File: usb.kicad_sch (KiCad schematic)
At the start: 7 parts, among them J3 USB_C_Plug, U2 STUSB03EQR

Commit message: *.kicad_sch: add CHIPSAlliance_ prefix for footprint
Signed-off-by: Huang Rui <vowstar@gmail.com>
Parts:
- U2: footprint Interface:QFN_B03EQR_STM -> CHIPSAlliance_Interface:QFN_B03EQR_STM
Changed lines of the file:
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@@
       (effects (font (size 1.524 1.524)))
     )
-    (property "Footprint" "Interface:QFN_B03EQR_STM" (at 76.2 100.33 0)
+    (property "Footprint" "CHIPSAlliance_Interface:QFN_B03EQR_STM" (at 76.2 100.33 0)
       (effects (font (size 1.524 1.524)) (justify left) hide)
     )

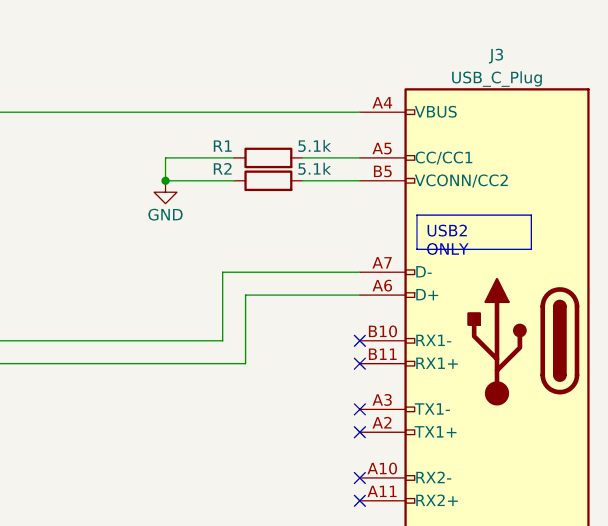
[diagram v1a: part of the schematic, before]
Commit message: library,uart*,usb*: fix usb connectors
Signed-off-by: Huang Rui <vowstar@gmail.com>
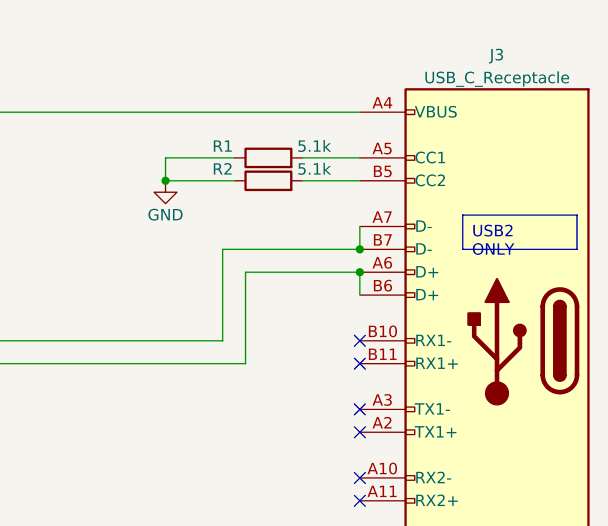
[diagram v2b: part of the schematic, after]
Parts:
- removed J3: USB_C_Plug, Connector_USB:USB_C_Receptacle_Molex_105450-0101, symbol CHIPSAlliance_Connector:USB_C_Plug
- added J3: USB_C_Receptacle, Connector_USB:USB_C_Receptacle_Molex_105450-0101, symbol CHIPSAlliance_Connector:USB_C_Receptacle
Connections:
- net D+: now also J3.A6 (D+), J3.B6 (D+)
- net D-: now also J3.A7 (D-), J3.B7 (D-)
- net GND: now also J3.A1 (GND), J3.A12 (GND), J3.B1 (GND), J3.B12 (GND), J3.S1 (SHIELD)
- net at R1.2: now also J3.A5 (CC1)
- net at C1.1, U2.14 (VBUS): now also J3.A4 (VBUS), J3.A9 (VBUS), J3.B4 (VBUS), J3.B9 (VBUS)
- net at R2.2: now also J3.B5 (CC2)

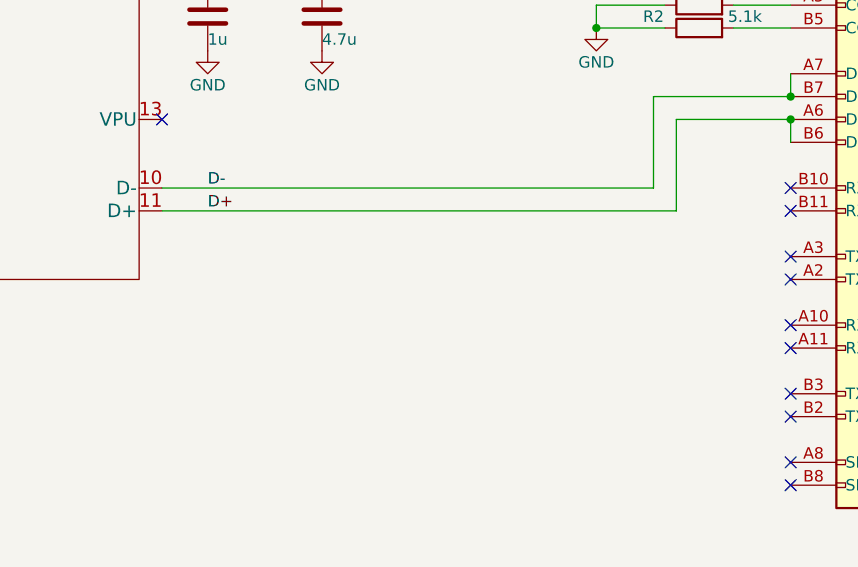
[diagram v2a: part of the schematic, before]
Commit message: {spi,uart,usb}.kicad_sch: add TPD4E02B04DQA as ESD protect
Signed-off-by: Huang Rui <vowstar@gmail.com>
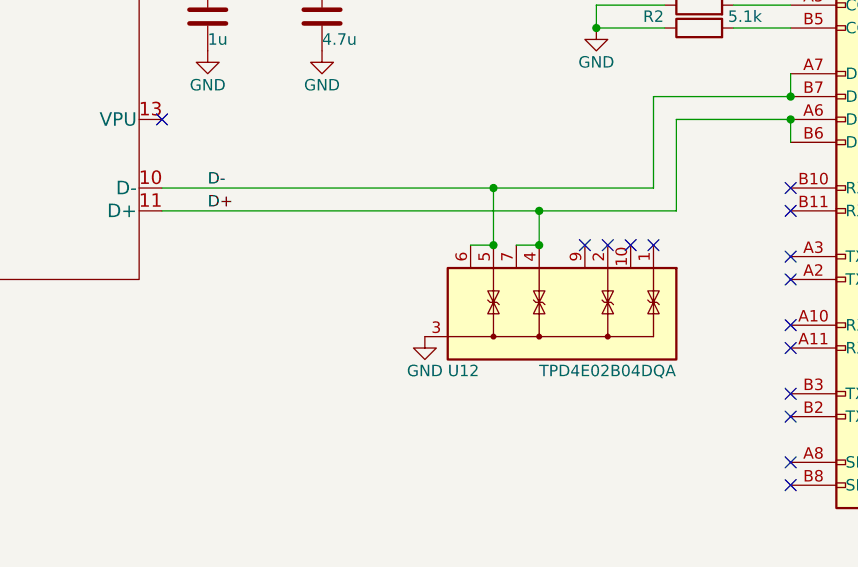
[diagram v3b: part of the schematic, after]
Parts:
- added U12: TPD4E02B04DQA, Package_SON:USON-10_2.5x1.0mm_P0.5mm, symbol Power_Protection:TPD4E02B04DQA
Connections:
- net D+: now also U12.4 (IO3), U12.7 (NC)
- net D-: now also U12.5 (IO4), U12.6 (NC)
- net GND: now also U12.3 (G), U12.8 (G)
- no-connect marks 11 -> 15
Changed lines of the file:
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@@
 (kicad_sch (version 20230121) (generator eeschema)
   (paper "A4")
+  (junction (at 151.13 92.71) (diameter 0) (color 0 0 0 0)
+  )
   (junction (at 67.31 60.96) (diameter 0) (color 0 0 0 0)
   )
+  (junction (at 151.13 88.9) (diameter 0) (color 0 0 0 0)
+  )
   (junction (at 63.5 60.96) (diameter 0) (color 0 0 0 0)
   )
@@
   (junction (at 179.07 78.74) (diameter 0) (color 0 0 0 0)
   )
+  (junction (at 146.05 86.36) (diameter 0) (color 0 0 0 0)
+  )
   (junction (at 157.48 68.58) (diameter 0) (color 0 0 0 0)
   )
   (junction (at 179.07 76.2) (diameter 0) (color 0 0 0 0)
   )
+  (junction (at 146.05 92.71) (diameter 0) (color 0 0 0 0)
+  )
   (junction (at 127 60.96) (diameter 0) (color 0 0 0 0)
   )
+  (no_connect (at 161.29 92.71))
   (no_connect (at 179.07 104.14))
+  (no_connect (at 158.75 92.71))
   (no_connect (at 179.07 111.76))
   (no_connect (at 179.07 96.52))
@@
   (no_connect (at 179.07 86.36))
   (no_connect (at 179.07 88.9))
+  (no_connect (at 156.21 92.71))
+  (no_connect (at 163.83 92.71))
   (no_connect (at 179.07 116.84))
   (bus_entry (at 50.8 88.9) (size 2.54 2.54)
@@
     (stroke (width 0) (type default))
   )
+  (wire (pts (xy 146.05 86.36) (xy 146.05 92.71))
+    (stroke (width 0) (type default))
+  )
   (wire (pts (xy 53.34 83.82) (xy 73.66 83.82))
     (stroke (width 0) (type default))
@@
     (stroke (width 0) (type default))
   )
+  (wire (pts (xy 143.51 92.71) (xy 146.05 92.71))
+    (stroke (width 0) (type default))
+  )
   (wire (pts (xy 67.31 60.96) (xy 73.66 60.96))
     (stroke (width 0) (type default))
@@
     (stroke (width 0) (type default))
   )
-  (wire (pts (xy 109.22 88.9) (xy 166.37 88.9))
+  (wire (pts (xy 109.22 88.9) (xy 151.13 88.9))
     (stroke (width 0) (type default))
   )
@@
     (stroke (width 0) (type default))
   )
+  (wire (pts (xy 151.13 88.9) (xy 166.37 88.9))
+    (stroke (width 0) (type default))
+  )
   (wire (pts (xy 67.31 63.5) (xy 73.66 63.5))
     (stroke (width 0) (type default))
@@
     (stroke (width 0) (type default))
   )
-  (wire (pts (xy 163.83 86.36) (xy 109.22 86.36))
+  (wire (pts (xy 148.59 92.71) (xy 151.13 92.71))
+    (stroke (width 0) (type default))
+  )
+  (wire (pts (xy 163.83 86.36) (xy 146.05 86.36))
     (stroke (width 0) (type default))
   )
@@
     (stroke (width 0) (type default))
   )
+  (wire (pts (xy 146.05 86.36) (xy 109.22 86.36))
+    (stroke (width 0) (type default))
+  )
   (bus (pts (xy 50.8 81.28) (xy 50.8 83.82))
     (stroke (width 0) (type default))
@@
   )
   (wire (pts (xy 53.34 88.9) (xy 73.66 88.9))
+    (stroke (width 0) (type default))
+  )
+  (wire (pts (xy 151.13 88.9) (xy 151.13 92.71))
     (stroke (width 0) (type default))
   )
@@
     )
   )
+  (symbol (lib_id "power:GND") (at 138.43 102.87 0) (unit 1)
+    (in_bom yes) (on_board yes) (dnp no)
+    (property "Reference" "#PWR02" (at 138.43 109.22 0)
+      (effects (font (size 1.27 1.27)) hide)
+    )
+    (property "Value" "GND" (at 138.43 106.68 0)
+      (effects (font (size 1.27 1.27)))
+    )
+    (property "Footprint" "" (at 138.43 102.87 0)
+      (effects (font (size 1.27 1.27)) hide)
+    )
+    (property "Datasheet" "" (at 138.43 102.87 0)
+      (effects (font (size 1.27 1.27)) hide)
+    )
+    (pin "1")
+    (instances
+      (project "fmc_usb_gpio_spi_jtag"
+        (path "/387bfcf1-ae49-4b85-be89-3bb02ce2e960/4338fda8-0ea2-4bf2-b1c2-c685ef11d6a0"
+          (reference "#PWR02") (unit 1)
+        )
+        (path "/387bfcf1-ae49-4b85-be89-3bb02ce2e960/4ff80468-3372-4da6-9aa6-0708696df1f4"
+          (reference "#PWR0235") (unit 1)
+        )
+        (path "/387bfcf1-ae49-4b85-be89-3bb02ce2e960/050a965f-1566-4fd5-8eeb-6ab96a9baeba"
+          (reference "#PWR0234") (unit 1)
+        )
+      )
+    )
+  )
   (symbol (lib_id "power:VDD") (at 63.5 60.96 0) (unit 1)
     (in_bom yes) (on_board yes) (dnp no)
@@
         )
       )
+    )
+  )
+  (symbol (lib_id "Power_Protection:TPD4E02B04DQA") (at 153.67 100.33 270) (unit 1)
+    (in_bom yes) (on_board yes) (dnp no)
+    (property "Reference" "U12" (at 140.97 106.68 90)
+      (effects (font (size 1.27 1.27)) (justify left))
+    )
+    (property "Value" "TPD4E02B04DQA" (at 151.13 106.68 90)
+      (effects (font (size 1.27 1.27)) (justify left))
+    )
+    (property "Footprint" "Package_SON:USON-10_2.5x1.0mm_P0.5mm" (at 153.67 107.95 0)
+      (effects (font (size 1.27 1.27)) (justify left) hide)
+    )
+    (property "Datasheet" "http://www.ti.com/lit/ds/symlink/tpd4e02b04.pdf" (at 153.67 102.87 0)
+      (effects (font (size 1.27 1.27)) hide)
+    )
+    (pin "3")
+    (pin "1")
+    (pin "10")
+    (pin "2")
+    (pin "4")
+    (pin "5")
+    (pin "6")
+    (pin "7")
+    (pin "8")
+    (pin "9")
+    (instances
+      (project "fmc_usb_gpio_spi_jtag"
+        (path "/387bfcf1-ae49-4b85-be89-3bb02ce2e960/050a965f-1566-4fd5-8eeb-6ab96a9baeba"
+          (reference "U12") (unit 1)
+        )
+        (path "/387bfcf1-ae49-4b85-be89-3bb02ce2e960/4ff80468-3372-4da6-9aa6-0708696df1f4"
+          (reference "U18") (unit 1)
+        )
+      )

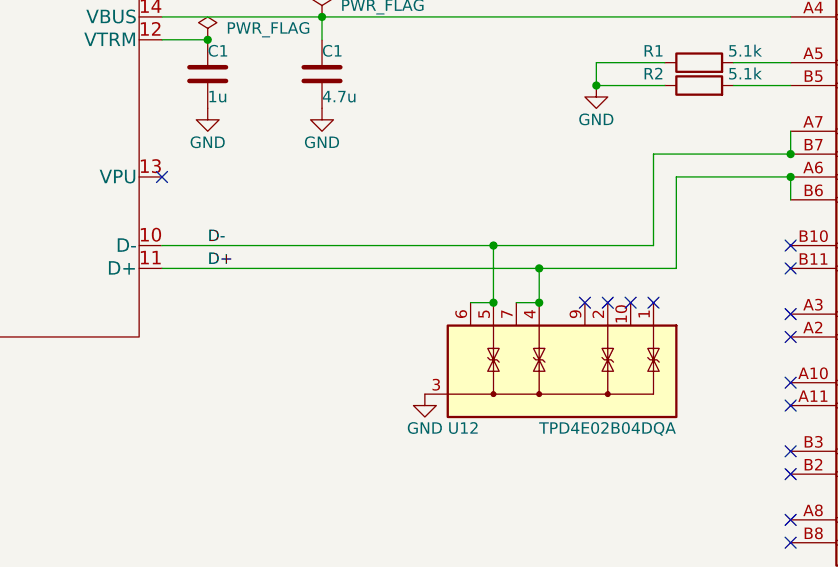
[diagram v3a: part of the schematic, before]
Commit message: usb.kicad_sch: swap D+ and D- of the ESD protection pin
Signed-off-by: Huang Rui <vowstar@gmail.com>
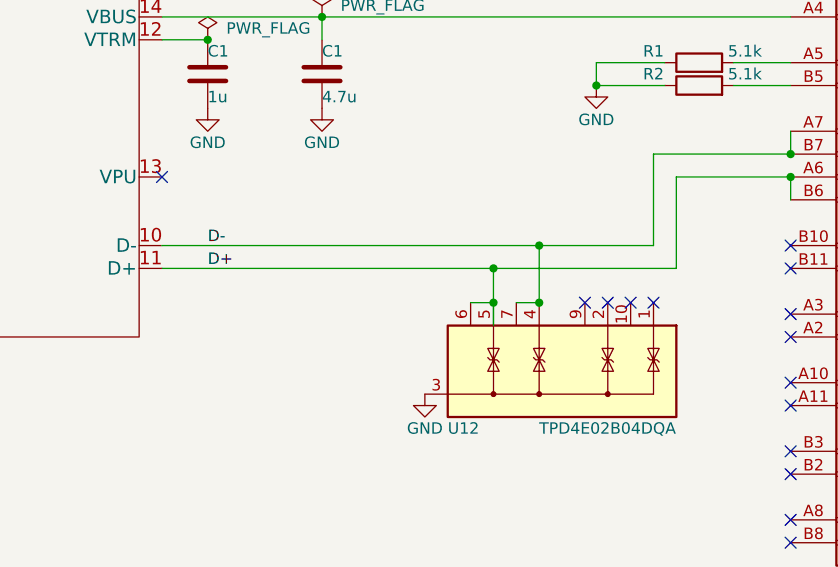
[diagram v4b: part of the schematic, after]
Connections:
- net D+: now also U12.5 (IO4), U12.6 (NC); no longer U12.4 (IO3), U12.7 (NC)
- net D-: now also U12.4 (IO3), U12.7 (NC); no longer U12.5 (IO4), U12.6 (NC)
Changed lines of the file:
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@@
 (kicad_sch (version 20230121) (generator eeschema)
   (paper "A4")
-  (junction (at 151.13 92.71) (diameter 0) (color 0 0 0 0)
-  )
   (junction (at 67.31 60.96) (diameter 0) (color 0 0 0 0)
   )
-  (junction (at 151.13 88.9) (diameter 0) (color 0 0 0 0)
+  (junction (at 146.05 88.9) (diameter 0) (color 0 0 0 0)
   )
   (junction (at 63.5 60.96) (diameter 0) (color 0 0 0 0)
@@
   (junction (at 179.07 78.74) (diameter 0) (color 0 0 0 0)
   )
-  (junction (at 146.05 86.36) (diameter 0) (color 0 0 0 0)
+  (junction (at 151.13 92.71) (diameter 0) (color 0 0 0 0)
+  )
+  (junction (at 151.13 86.36) (diameter 0) (color 0 0 0 0)
   )
   (junction (at 157.48 68.58) (diameter 0) (color 0 0 0 0)
@@
     (stroke (width 0) (type default))
   )
-  (wire (pts (xy 146.05 86.36) (xy 146.05 92.71))
+  (wire (pts (xy 146.05 88.9) (xy 146.05 92.71))
     (stroke (width 0) (type default))
   )
@@
     (stroke (width 0) (type default))
   )
+  (wire (pts (xy 146.05 95.25) (xy 146.05 92.71))
+    (stroke (width 0) (type default))
+  )
   (wire (pts (xy 143.51 92.71) (xy 146.05 92.71))
     (stroke (width 0) (type default))
@@
     (stroke (width 0) (type default))
   )
-  (wire (pts (xy 109.22 88.9) (xy 151.13 88.9))
+  (wire (pts (xy 109.22 88.9) (xy 146.05 88.9))
     (stroke (width 0) (type default))
   )
@@
     (stroke (width 0) (type default))
   )
-  (wire (pts (xy 151.13 88.9) (xy 166.37 88.9))
+  (wire (pts (xy 148.59 92.71) (xy 151.13 92.71))
+    (stroke (width 0) (type default))
+  )
+  (wire (pts (xy 151.13 86.36) (xy 151.13 92.71))
     (stroke (width 0) (type default))
   )
@@
     (stroke (width 0) (type default))
   )
-  (wire (pts (xy 148.59 92.71) (xy 151.13 92.71))
-    (stroke (width 0) (type default))
-  )
-  (wire (pts (xy 163.83 86.36) (xy 146.05 86.36))
+  (wire (pts (xy 146.05 88.9) (xy 166.37 88.9))
     (stroke (width 0) (type default))
   )
@@
     (stroke (width 0) (type default))
   )
-  (wire (pts (xy 146.05 86.36) (xy 109.22 86.36))
+  (wire (pts (xy 109.22 86.36) (xy 151.13 86.36))
     (stroke (width 0) (type default))
   )
@@
     (stroke (width 0) (type default))
   )
+  (wire (pts (xy 151.13 86.36) (xy 163.83 86.36))
+    (stroke (width 0) (type default))
+  )
   (wire (pts (xy 157.48 68.58) (xy 165.1 68.58))
     (stroke (width 0) (type default))
@@
     (stroke (width 0) (type default))
   )
-  (wire (pts (xy 151.13 88.9) (xy 151.13 92.71))
-    (stroke (width 0) (type default))
-  )

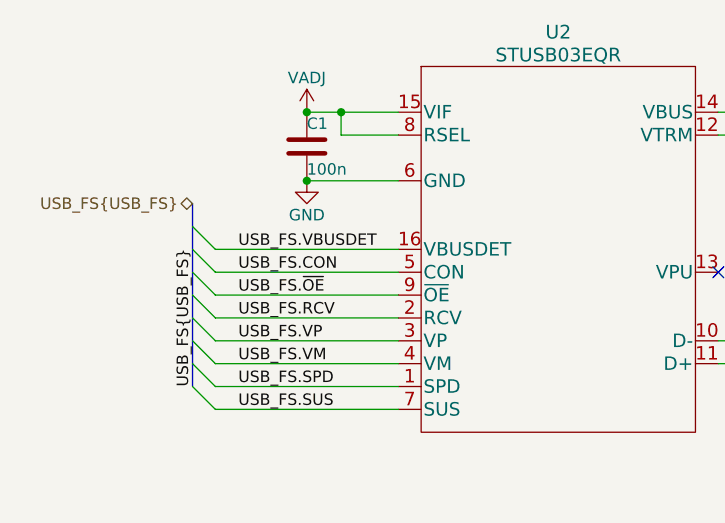
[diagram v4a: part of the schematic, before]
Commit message: *.kicad_sch: rename VBUSDET to DET, save schematic space
Signed-off-by: Huang Rui <vowstar@gmail.com>
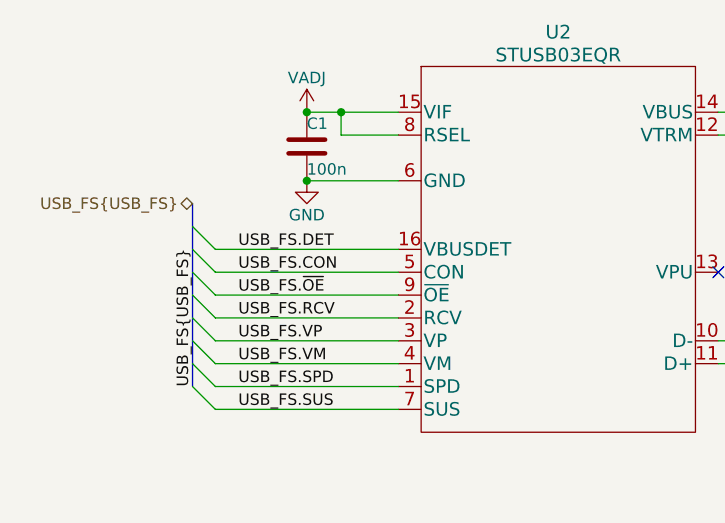
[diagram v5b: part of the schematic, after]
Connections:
- net USB_FS.VBUSDET renamed USB_FS.DET
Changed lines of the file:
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@@
     (effects (font (size 1.27 1.27)) (justify left bottom))
   )
-  (label "USB_FS.VBUSDET" (at 55.88 76.2 0) (fields_autoplaced)
+  (label "USB_FS.DET" (at 55.88 76.2 0) (fields_autoplaced)
     (effects (font (size 1.27 1.27)) (justify left bottom))
   )
